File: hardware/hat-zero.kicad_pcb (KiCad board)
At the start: 4 copper layers, 65 x 30.6 mm, 44 parts, among them J101 Boot, J102 Raspberry_Pi_Zero, P101 Debug, P201 CON-SENSOR2, P202 CON-SENSOR2, P203 CON-SENSOR2, P204 CON-SENSOR2, U101 XMC1100, U102 LD1117, U201 74AHC244, U202 74AHC244

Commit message: add sym table and pcb hint
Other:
- board text added: "Ringe"
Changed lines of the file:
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@@
   (general
     (thickness 1.6)
-    (drawings 11)
+    (drawings 12)
     (tracks 871)
     (zones 0)
@@
       (clearance 0.65024))
   )
+  (gr_text Ringe (at 174.2 67.25) (layer Dwgs.User)
+    (effects (font (size 2.032 1.524) (thickness 0.3048)))
+  )
   (gr_text tinkerforge.com (at 157.3 53.3) (layer F.SilkS)

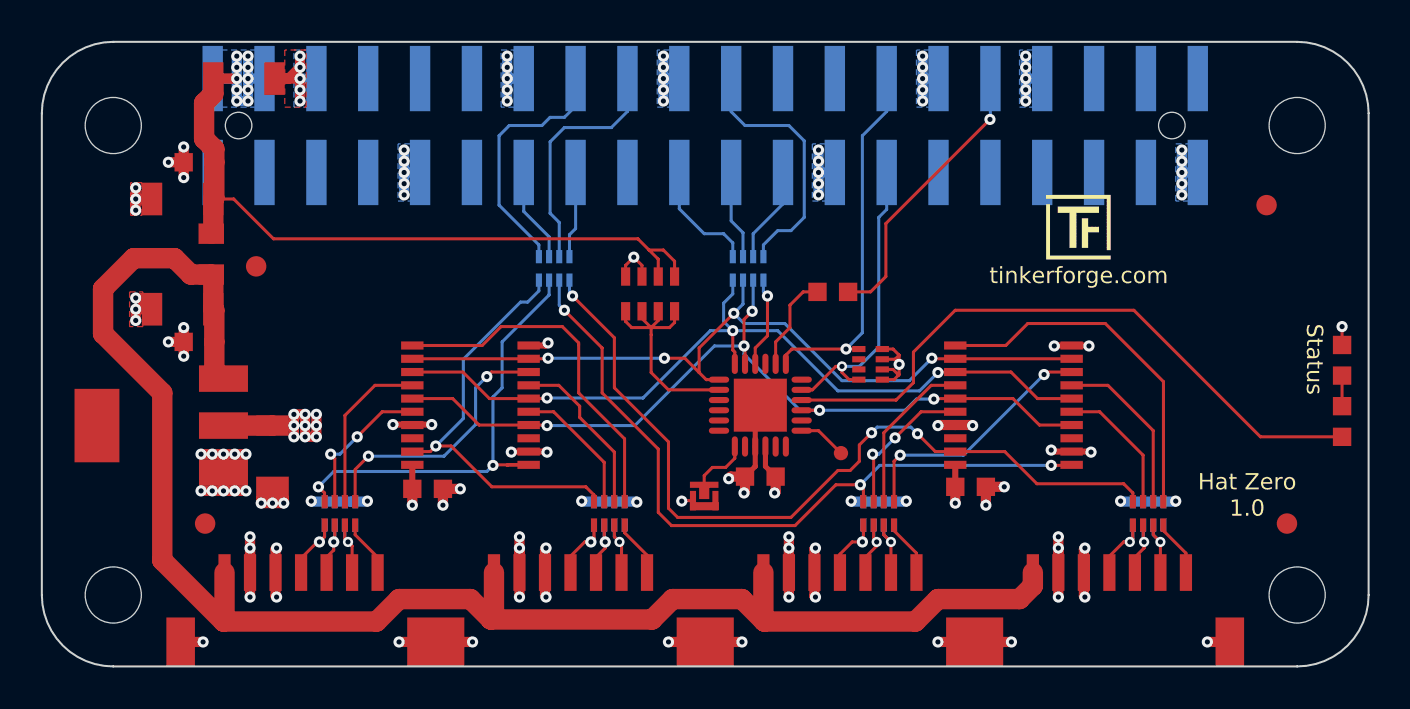
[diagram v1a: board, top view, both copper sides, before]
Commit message: fix graphical elements
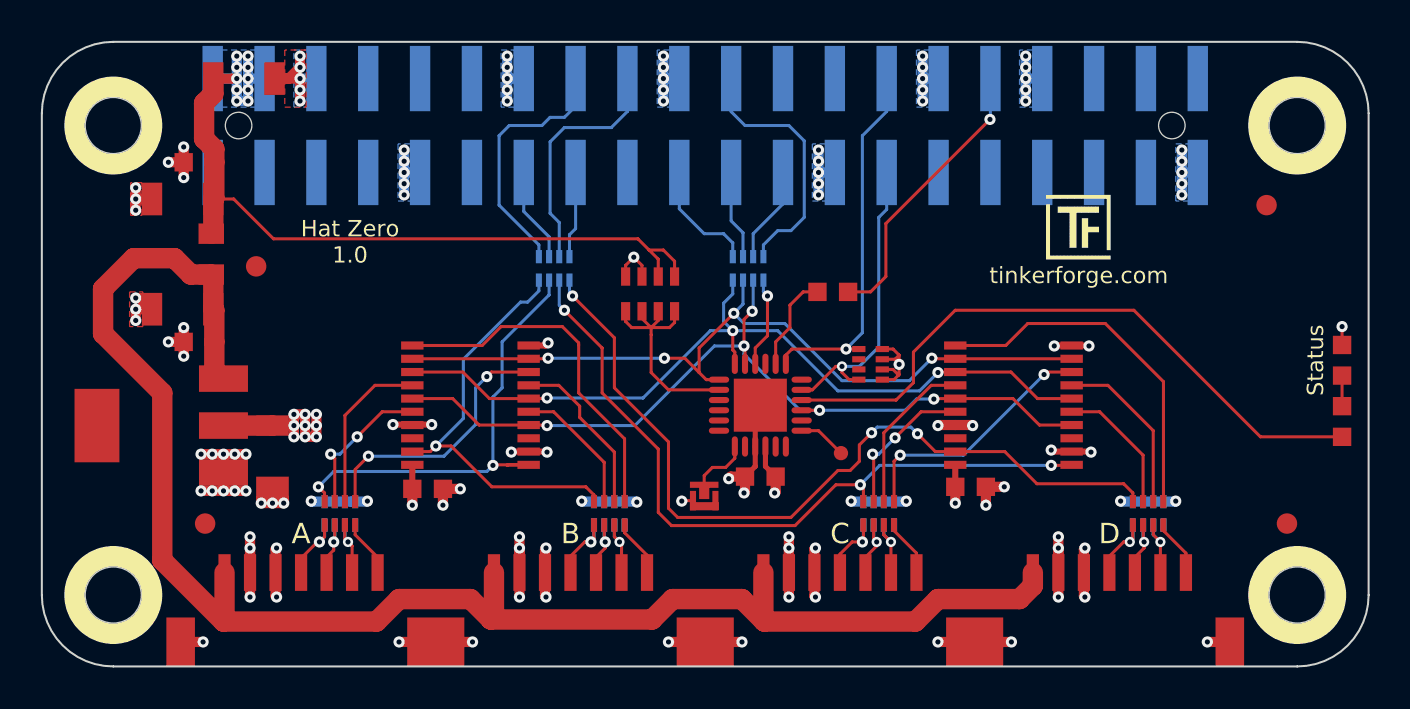
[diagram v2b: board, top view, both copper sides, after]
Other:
- board text added: "A"
- board text added: "B"
- board text added: "C"
- board text added: "D"
- board text removed: "Ringe"
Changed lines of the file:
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@@
   (general
     (thickness 1.6)
-    (drawings 12)
+    (drawings 23)
     (tracks 871)
     (zones 0)
@@
     (zone_45_only no)
     (trace_min 0.15)
-    (segment_width 0.381)
+    (segment_width 1)
     (edge_width 0.09906)
     (via_size 0.55)
@@
       (clearance 0.65024))
   )
-  (gr_text Ringe (at 174.2 67.25) (layer Dwgs.User)
-    (effects (font (size 2.032 1.524) (thickness 0.3048)))
+  (gr_circle (center 168 68.95) (end 169.9 68.95) (layer B.SilkS) (width 1))
+  (gr_circle (center 168 45.95) (end 169.9 45.95) (layer B.SilkS) (width 1))
+  (gr_circle (center 110 45.95) (end 111.9 45.95) (layer B.SilkS) (width 1))
+  (gr_circle (center 110 68.95) (end 111.9 68.95) (layer B.SilkS) (width 1))
+  (gr_circle (center 110 68.95) (end 111.9 68.95) (layer F.SilkS) (width 1))
+  (gr_circle (center 110 45.95) (end 111.9 45.95) (layer F.SilkS) (width 1))
+  (gr_circle (center 168 45.95) (end 169.9 45.95) (layer F.SilkS) (width 1))
+  (gr_circle (center 168 68.95) (end 169.9 68.95) (layer F.SilkS) (width 1))
+  (gr_text D (at 158.8 65.95) (layer F.SilkS)
+    (effects (font (size 1 1) (thickness 0.15)))
+  )
+  (gr_text C (at 145.6 65.95) (layer F.SilkS)
+    (effects (font (size 1 1) (thickness 0.15)))
+  )
+  (gr_text B (at 132.4 65.95) (layer F.SilkS)
+    (effects (font (size 1 1) (thickness 0.15)))
+  )
+  (gr_text A (at 119.2 65.95) (layer F.SilkS)
+    (effects (font (size 1 1) (thickness 0.15)))
   )
   (gr_text tinkerforge.com (at 157.3 53.3) (layer F.SilkS)
     (effects (font (size 0.8 0.8) (thickness 0.15)))
   )
-  (gr_text "Hat Zero\n1.0" (at 165.55 64.05) (layer F.SilkS)
+  (gr_text "Hat Zero\n1.0" (at 121.6 51.65) (layer F.SilkS)
     (effects (font (size 0.8 0.8) (thickness 0.15)))
   )
-  (gr_text Status (at 168.85 57.4 270) (layer F.SilkS)
+  (gr_text Status (at 168.9 57.45 90) (layer F.SilkS)
     (effects (font (size 0.8 0.8) (thickness 0.15)))
   )

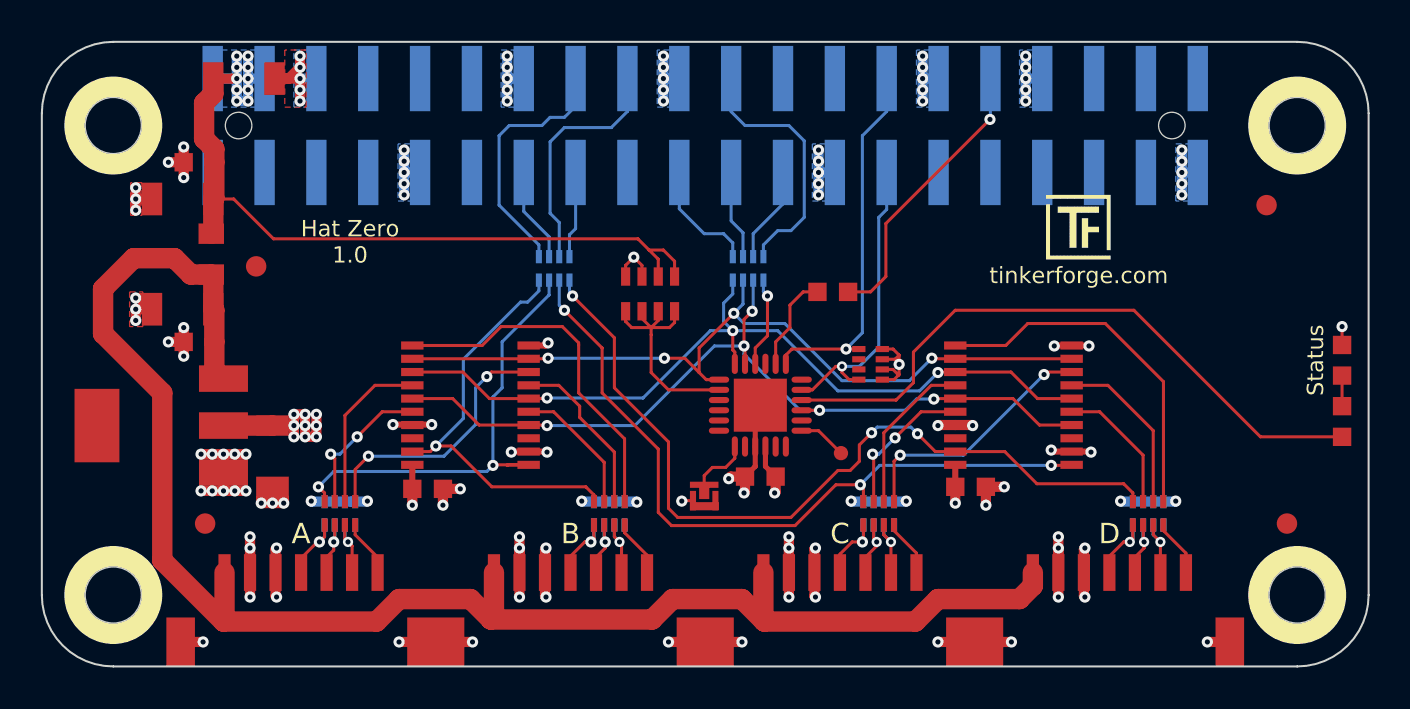
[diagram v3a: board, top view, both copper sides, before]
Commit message: changed pcb layout to single sided placement, added clock pullup's, changed symlib-table
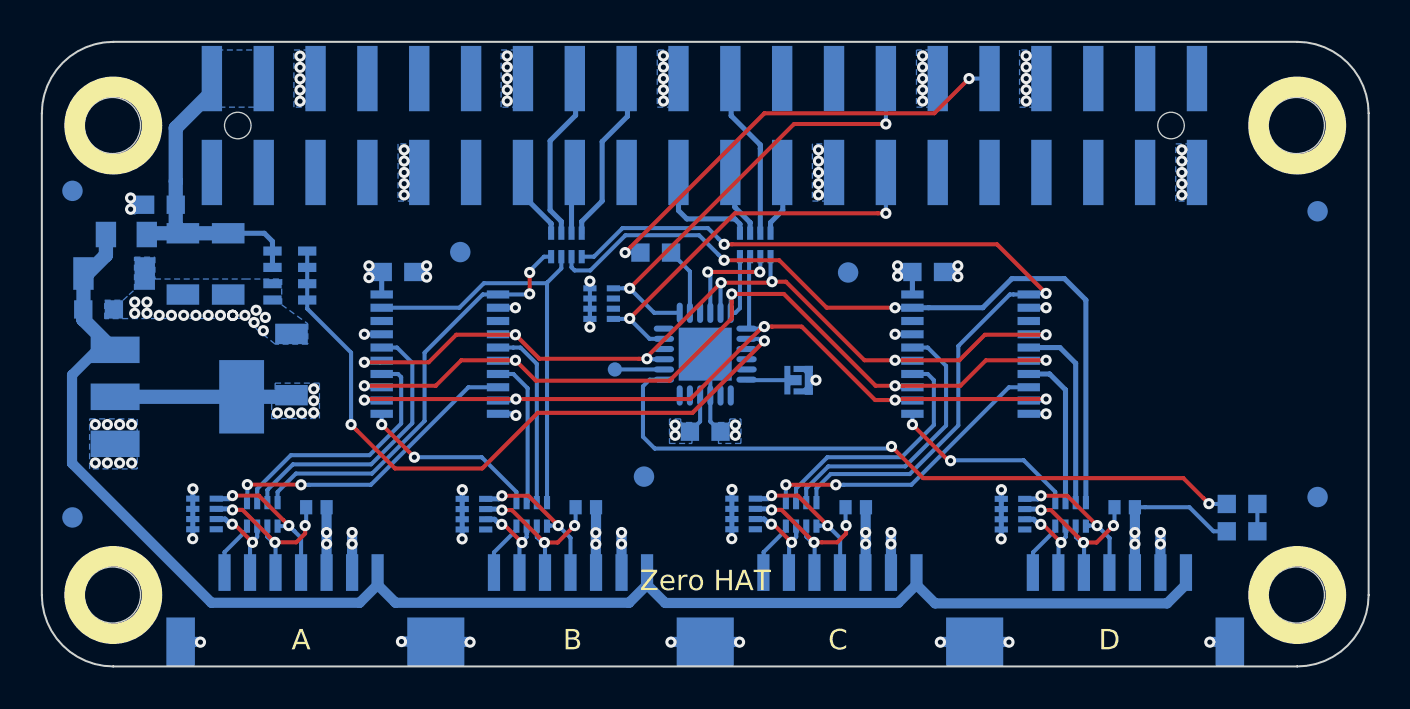
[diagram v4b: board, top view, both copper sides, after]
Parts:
- removed the Fiducial_Mark at (167.5, 65.5)
- removed the Fiducial_Mark at (114.5, 65.5)
- removed the Fiducial_Mark at (166.5, 49.9)
- removed the Fiducial_Mark at (117.0, 52.9)
- removed G***: LOGO, kicad-libraries:Logo_CoMCU
- removed G***: Logo_31x31, kicad-libraries:Logo_31x31
- removed VAL: CE_5mm, kicad-libraries:CE_5mm
- removed VAL: WEEE_7mm, kicad-libraries:WEEE_7mm
- added Fiducial_Mark: VAL**, kicad-libraries:Fiducial_Mark, F.Cu at (169.0, 50.1)
- added Fiducial_Mark: VAL**, kicad-libraries:Fiducial_Mark, F.Cu at (169.0, 64.2)
- added Fiducial_Mark: VAL**, kicad-libraries:Fiducial_Mark, F.Cu at (108.0, 65.2)
- added Fiducial_Mark: VAL**, kicad-libraries:Fiducial_Mark, F.Cu at (108.0, 49.1)
- added Fiducial_Mark: VAL**, kicad-libraries:Fiducial_Mark, F.Cu at (127.0, 52.1)
- added Fiducial_Mark: VAL**, kicad-libraries:Fiducial_Mark, F.Cu at (136.0, 63.1)
- added Fiducial_Mark: VAL**, kicad-libraries:Fiducial_Mark, F.Cu at (146.0, 53.1)
- added R1: 100k, kicad-libraries:R0402F, B.Cu at (120.0, 64.7)
- added R2: 100k, kicad-libraries:R0402F, B.Cu at (133.2, 64.7)
- added R3: 100k, kicad-libraries:R0402F, B.Cu at (146.4, 64.7)
- added R4: 100k, kicad-libraries:R0402F, B.Cu at (159.6, 64.7)
- C101, C102, C103, C104, C105, C106, C107, C201, C202, D101, J101, L101, P101, P201, P202, P203, P204, R101, R102, RP102, RP103, RP201, RP202, RP203, RP204, U101, U102, U201, U202: moved to B.Cu
- moved RP102 17.7 mm to (118.7, 53.3), turned to 90 degrees
- moved RP103 13.5 mm to (133.9, 54.7)
- moved P101 11.8 mm to (134.6, 57.9)
- moved C201 10.7 mm to (149.9, 53.1)
- moved C202 10.7 mm to (124.0, 53.1)
- moved D101 9.71 mm to (165.3, 65.8), turned to 0 degrees
- moved C105 9.56 mm to (113.4, 52.7), turned to 90 degrees
- moved R101 8.89 mm to (136.6, 52.2), turned to 180 degrees
- moved J101 7.32 mm to (143.6, 58.4), turned to 180 degrees
- moved CP202 6.63 mm to (127.7, 65.0), turned to 270 degrees
- moved CP201 6.63 mm to (114.5, 65.0), turned to 270 degrees
- moved CP204 6.62 mm to (154.1, 65.0), turned to 270 degrees
- moved CP203 6.62 mm to (140.9, 65.0), turned to 270 degrees
- moved R102 6.35 mm to (165.3, 64.5), turned to 180 degrees
- moved C104 5.17 mm to (109.3, 55.0), turned to 0 degrees
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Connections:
- CP201 pad 1: (no net) -> Net-(CP201-Pad1)
- CP202 pad 1: (no net) -> Net-(CP202-Pad1)
- CP203 pad 1: (no net) -> Net-(CP203-Pad1)
- CP204 pad 1: (no net) -> Net-(CP204-Pad1)
- J102 pad 1: (no net) -> Net-(J102-Pad1)
- J102 pad 10: (no net) -> Net-(J102-Pad10)
- J102 pad 11: (no net) -> Net-(J102-Pad11)
- J102 pad 12: (no net) -> Net-(J102-Pad12)
- J102 pad 17: (no net) -> Net-(J102-Pad17)
- J102 pad 24: (no net) -> Net-(J102-Pad24)
- J102 pad 26: (no net) -> Net-(J102-Pad26)
- J102 pad 29: (no net) -> Net-(J102-Pad29)
- J102 pad 3: (no net) -> Net-(J102-Pad3)
- J102 pad 31: (no net) -> Net-(J102-Pad31)
- J102 pad 33: (no net) -> Net-(J102-Pad33)
- J102 pad 35: (no net) -> Net-(J102-Pad35)
- J102 pad 36: (no net) -> Net-(J102-Pad36)
- J102 pad 37: (no net) -> Net-(J102-Pad37)
- J102 pad 38: (no net) -> Net-(J102-Pad38)
- J102 pad 40: (no net) -> Net-(J102-Pad40)
- J102 pad 5: (no net) -> Net-(J102-Pad5)
- J102 pad 7: (no net) -> Net-(J102-Pad7)
- J102 pad 8: (no net) -> Net-(J102-Pad8)
- P201 pad 4: Net-(CP201-Pad4) -> Net-(CP201-Pad1)
- P201 pad 5: Net-(CP201-Pad3) -> Net-(CP201-Pad2)
- P201 pad 6: Net-(CP201-Pad2) -> Net-(CP201-Pad3)
- P202 pad 4: Net-(CP202-Pad4) -> Net-(CP202-Pad1)
- P202 pad 5: Net-(CP202-Pad3) -> Net-(CP202-Pad2)
- P202 pad 6: Net-(CP202-Pad2) -> Net-(CP202-Pad3)
- P203 pad 4: Net-(CP203-Pad4) -> Net-(CP203-Pad1)
- P203 pad 5: Net-(CP203-Pad3) -> Net-(CP203-Pad2)
- P203 pad 6: Net-(CP203-Pad2) -> Net-(CP203-Pad3)
- P204 pad 4: Net-(CP204-Pad4) -> Net-(CP204-Pad1)
- P204 pad 5: Net-(CP204-Pad3) -> Net-(CP204-Pad2)
- P204 pad 6: Net-(CP204-Pad2) -> Net-(CP204-Pad3)
- RP102 pad 5: GND -> +5V
- RP102 pad 6: GND -> +5V
- RP102 pad 7: +5V -> GND
- RP102 pad 8: +5V -> GND
- RP103 pad 6: (no net) -> Net-(RP103-Pad6)
- RP103 pad 7: (no net) -> Net-(RP103-Pad7)
- RP104 pad 1: B-CS3 -> B-CS2
- RP104 pad 2: B-CS2 -> B-CS3
- RP104 pad 3: B-CS0 -> B-CS1
- RP104 pad 4: B-CS1 -> B-CS0
- RP104 pad 5: Net-(J102-Pad16) -> Net-(J102-Pad13)
- RP104 pad 6: Net-(J102-Pad13) -> Net-(J102-Pad16)
- RP104 pad 7: Net-(J102-Pad18) -> Net-(J102-Pad15)
- RP104 pad 8: Net-(J102-Pad15) -> Net-(J102-Pad18)
- RP106 pad 1: B-CS4 -> B-CLK
- RP106 pad 2: B-CLK -> B-CS4
- RP106 pad 7: Net-(J102-Pad23) -> Net-(J102-Pad22)
- RP106 pad 8: Net-(J102-Pad22) -> Net-(J102-Pad23)
- RP201 pad 1: Net-(CP201-Pad4) -> Net-(CP201-Pad1)
- RP201 pad 2: Net-(CP201-Pad3) -> Net-(CP201-Pad2)
- RP201 pad 3: Net-(CP201-Pad2) -> Net-(CP201-Pad3)
- RP202 pad 1: Net-(CP202-Pad4) -> Net-(CP202-Pad1)
- RP202 pad 2: Net-(CP202-Pad3) -> Net-(CP202-Pad2)
- RP202 pad 3: Net-(CP202-Pad2) -> Net-(CP202-Pad3)
- RP203 pad 1: Net-(CP203-Pad4) -> Net-(CP203-Pad1)
- RP203 pad 2: Net-(CP203-Pad3) -> Net-(CP203-Pad2)
- RP203 pad 3: Net-(CP203-Pad2) -> Net-(CP203-Pad3)
- RP204 pad 1: Net-(CP204-Pad4) -> Net-(CP204-Pad1)
- RP204 pad 2: Net-(CP204-Pad3) -> Net-(CP204-Pad2)
- RP204 pad 3: Net-(CP204-Pad2) -> Net-(CP204-Pad3)
- U101 pad 11: (no net) -> Net-(U101-Pad11)
- U101 pad 12: (no net) -> Net-(U101-Pad12)
- U101 pad 13: Net-(P101-Pad1) -> Net-(R102-Pad2)
- U101 pad 14: (no net) -> Net-(P101-Pad1)
- U101 pad 16: Net-(R102-Pad2) -> Net-(U101-Pad16)
- U101 pad 18: (no net) -> Net-(U101-Pad18)
- U101 pad 21: (no net) -> Net-(U101-Pad21)
- U101 pad 3: (no net) -> Net-(U101-Pad3)
- U101 pad 4: (no net) -> Net-(U101-Pad4)
- U101 pad 5: (no net) -> Net-(U101-Pad5)
- U101 pad 6: (no net) -> Net-(J101-Pad2)
- U101 pad 7: Net-(J101-Pad2) -> Net-(U101-Pad7)
- U101 pad 8: (no net) -> Net-(U101-Pad8)
- U201 pad 18: (no net) -> Net-(U201-Pad18)
- U201 pad 3: (no net) -> Net-(U201-Pad3)
- U202 pad 18: (no net) -> Net-(U202-Pad18)
- U202 pad 3: (no net) -> Net-(U202-Pad3)
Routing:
- net GND: track 109.5 -> 45.7 mm, vias 112 -> 105
- net +5V: track 42.2 -> 16.1 mm, vias 10 -> 0
- net IN-VOLTAGE: track 11.6 -> 34.1 mm, vias 0 -> 2
- net B-3V3: track 29.5 -> 38.9 mm
- net Net-(RP202-Pad5): track 17.6 -> 9.02 mm, vias 0 -> 2
- net Net-(RP204-Pad5): track 17.7 -> 9.44 mm, vias 0 -> 2
- net Net-(J102-Pad32): track 14.0 -> 22.1 mm, vias 1 -> 2
- net Net-(CP203-Pad1): track 0.00 -> 8.15 mm, vias 0 -> 2
- net Net-(CP202-Pad1): track 0.00 -> 7.52 mm, vias 0 -> 2
- net Net-(CP204-Pad1): track 0.00 -> 7.51 mm, vias 0 -> 2
- net Net-(CP201-Pad1): track 0.00 -> 7.34 mm, vias 0 -> 2
- net B-CS2: track 36.0 -> 42.8 mm, vias 3 -> 2
- net Net-(RP201-Pad7): track 7.27 -> 13.8 mm, vias 2 -> 0
- net Net-(RP203-Pad7): track 7.26 -> 13.8 mm, vias 2 -> 0
- net B-MOSI: track 40.9 -> 46.7 mm, vias 3 -> 5
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- added copper zone on B.Cu, net B-3V3
- removed copper zone on F.Cu, net GND
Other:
- net class Default: clearance 0.15 -> 0.149
- rule trace_clearance: 0.15 -> 0.149
- board text added: "Zero HAT"
- board text removed: "Hat Zero 1.0"
- board text removed: "tinkerforge.com"

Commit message: add logo
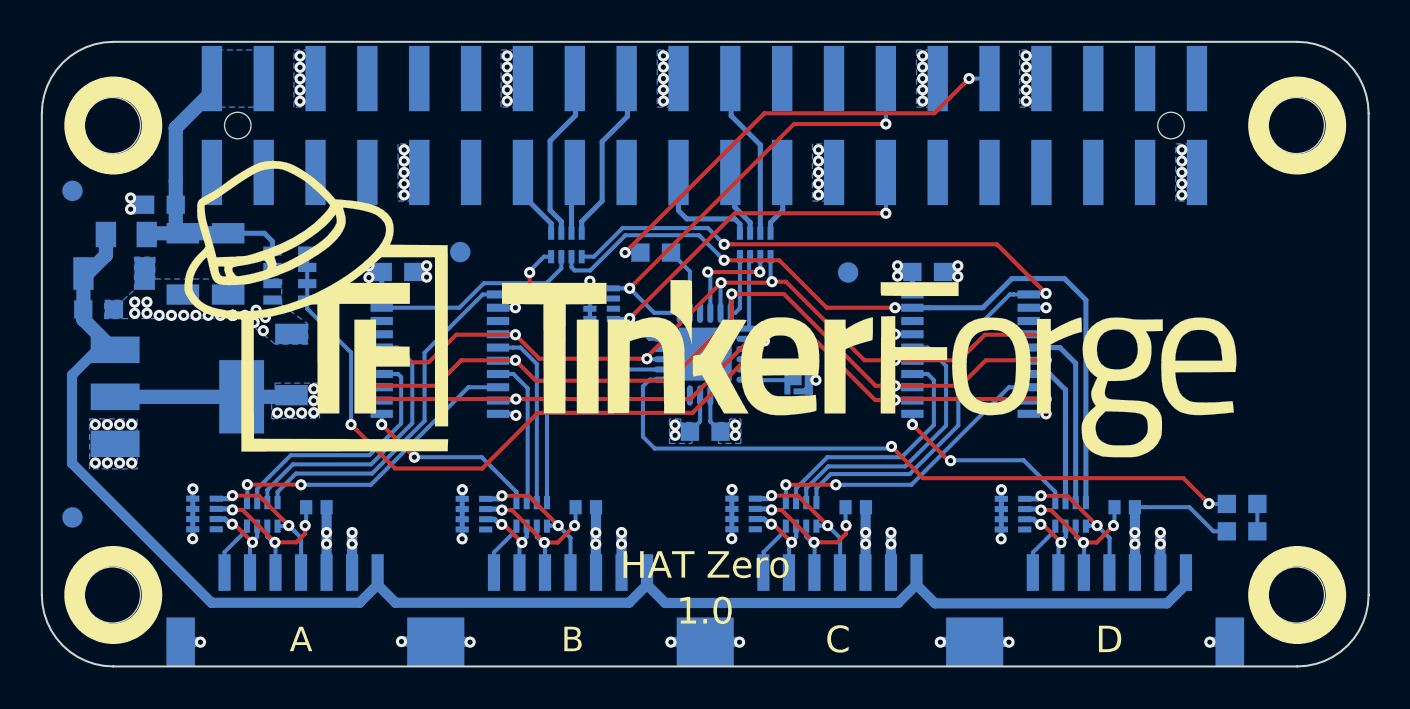
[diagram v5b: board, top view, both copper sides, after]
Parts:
- removed the Fiducial_Mark at (169.0, 50.1)
- removed the Fiducial_Mark at (169.0, 64.2)
- removed the Fiducial_Mark at (136.0, 63.1)
- added G***: LOGO, kicad-libraries:LOGO_TF_HAT, F.Cu at (139.1, 54.9)
- added G***: LOGO, kicad-libraries:Logo_31x31, B.Cu at (133.2, 60.3)
- added G***: LOGO, kicad-libraries:Logo_CoMCU, B.Cu at (167.5, 58.4)
- added VAL: CE_5mm, kicad-libraries:CE_5mm, B.Cu at (167.6, 52.0)
- added VAL: WEEE_7mm, kicad-libraries:WEEE_7mm, B.Cu at (160.2, 56.7)
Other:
- board text added: "1.0"
- board text added: "HAT Zero"
- board text added: "tinkerforge.com"
- board text removed: "Zero HAT"
